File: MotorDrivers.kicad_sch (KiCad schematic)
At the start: 0 parts

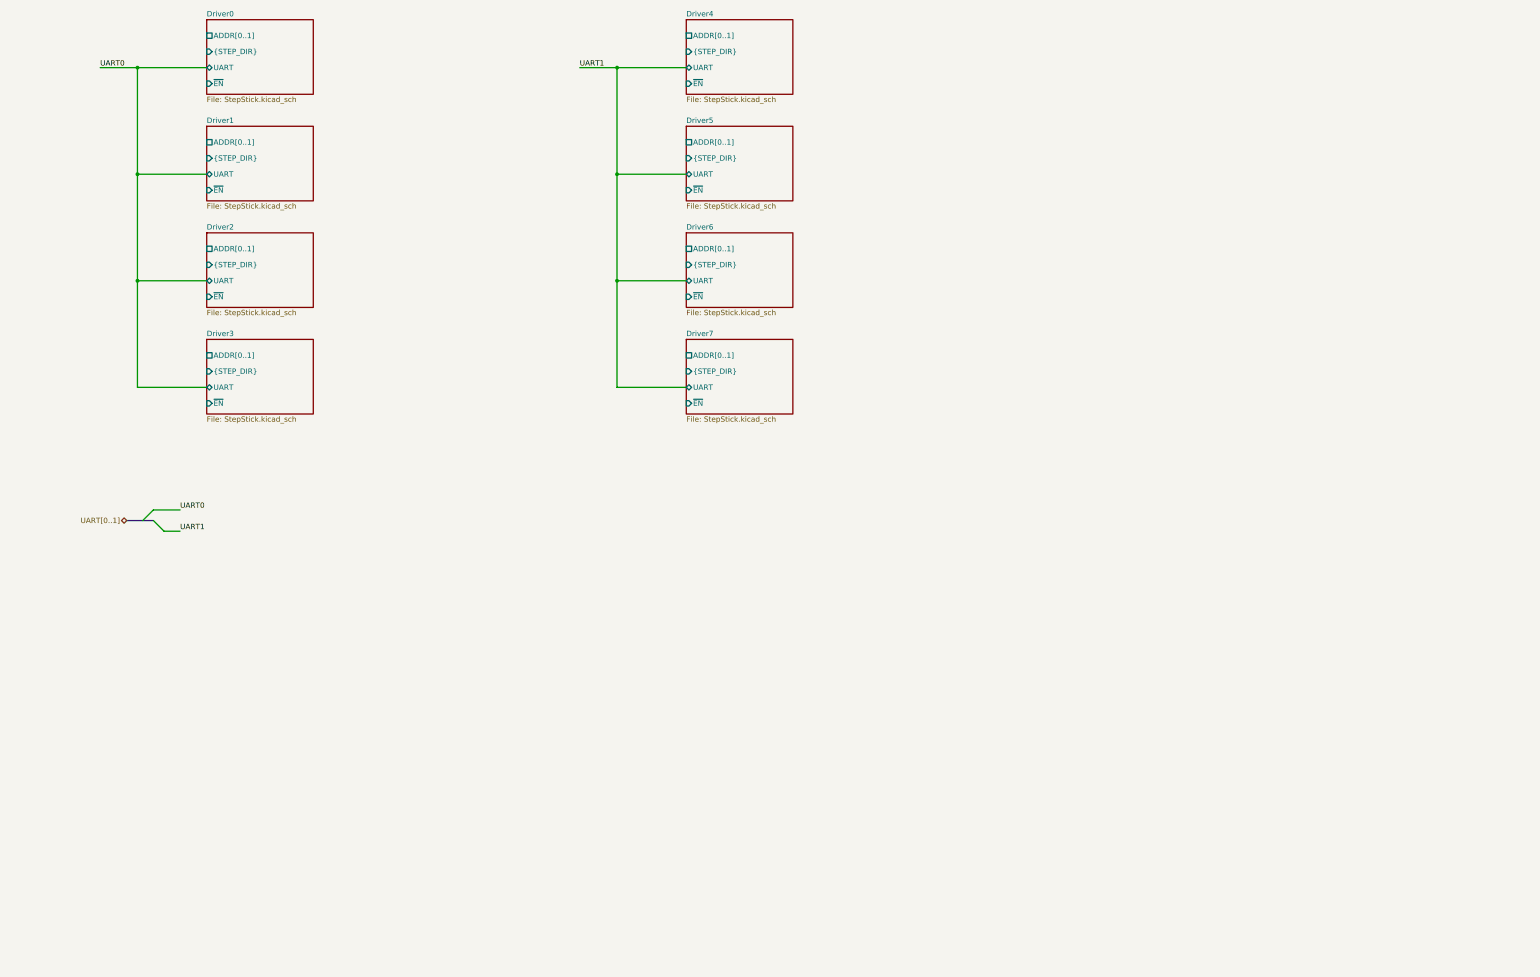
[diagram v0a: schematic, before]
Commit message: Increase text size, redo bus labels
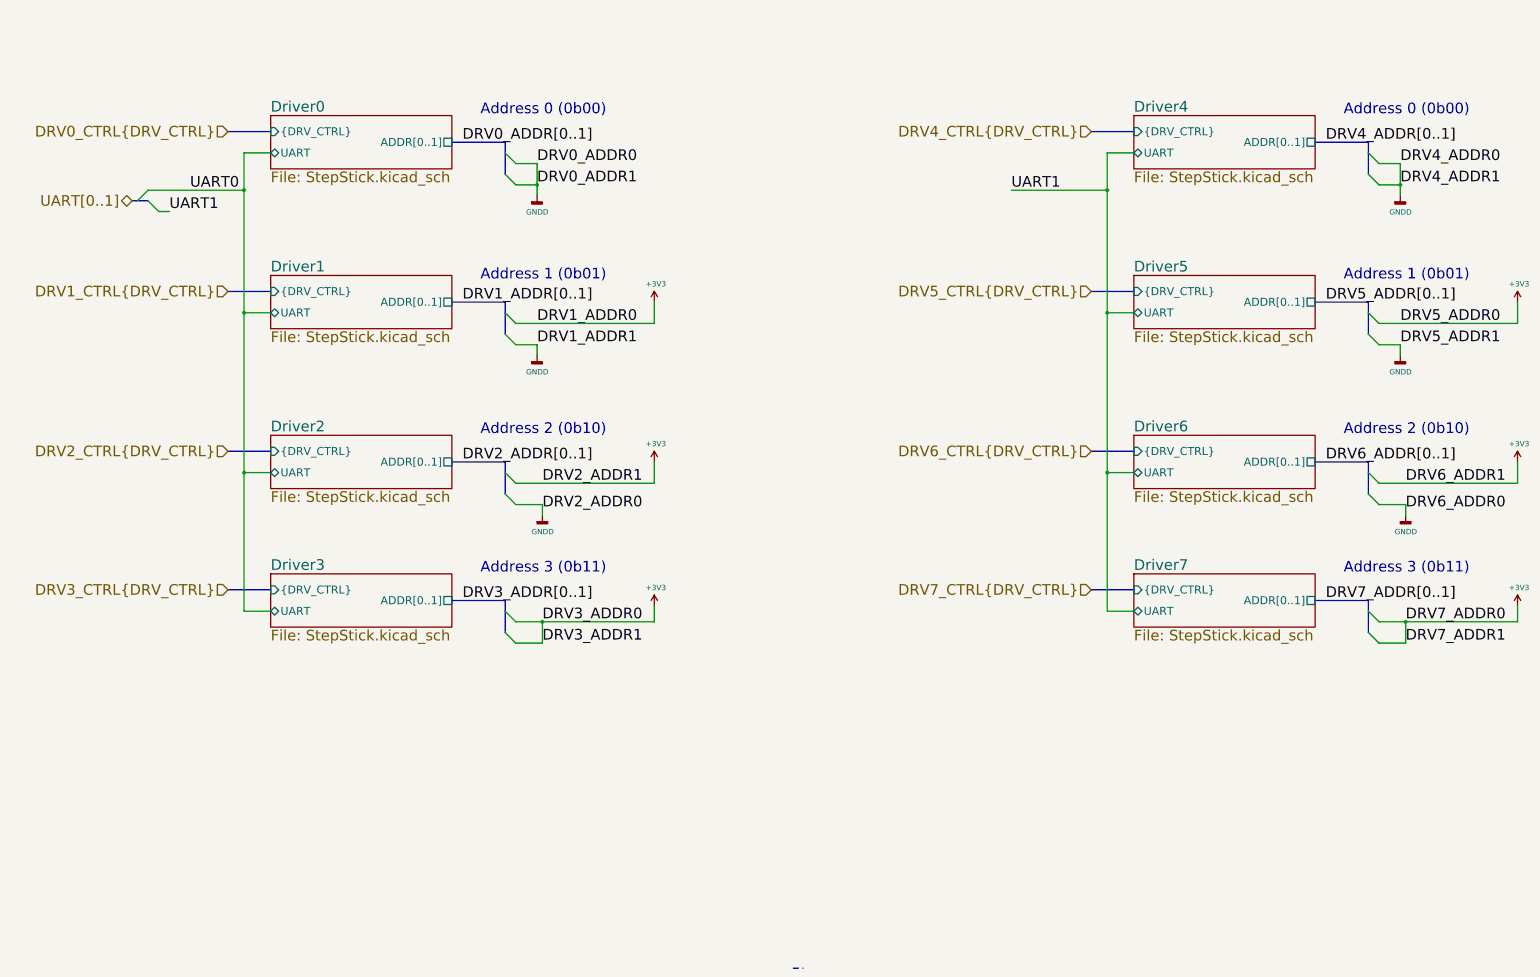
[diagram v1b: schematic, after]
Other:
- sheet Driver0 ports: added {DRV_CTRL}; removed {STEP_DIR}, ~EN
- sheet Driver1 ports: added {DRV_CTRL}; removed {STEP_DIR}, ~EN
- sheet Driver2 ports: added {DRV_CTRL}; removed {STEP_DIR}, ~EN
- sheet Driver3 ports: added {DRV_CTRL}; removed {STEP_DIR}, ~EN
- sheet Driver4 ports: added {DRV_CTRL}; removed {STEP_DIR}, ~EN
- sheet Driver5 ports: added {DRV_CTRL}; removed {STEP_DIR}, ~EN
- sheet Driver6 ports: added {DRV_CTRL}; removed {STEP_DIR}, ~EN
- sheet Driver7 ports: added {DRV_CTRL}; removed {STEP_DIR}, ~EN
- note added: "Address 0 (0b00)"
- note added: "Address 1 (0b01)"
- note added: "Address 2 (0b10)"
- note added: "Address 3 (0b11)"

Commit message: Configure driver chip address with jumpers
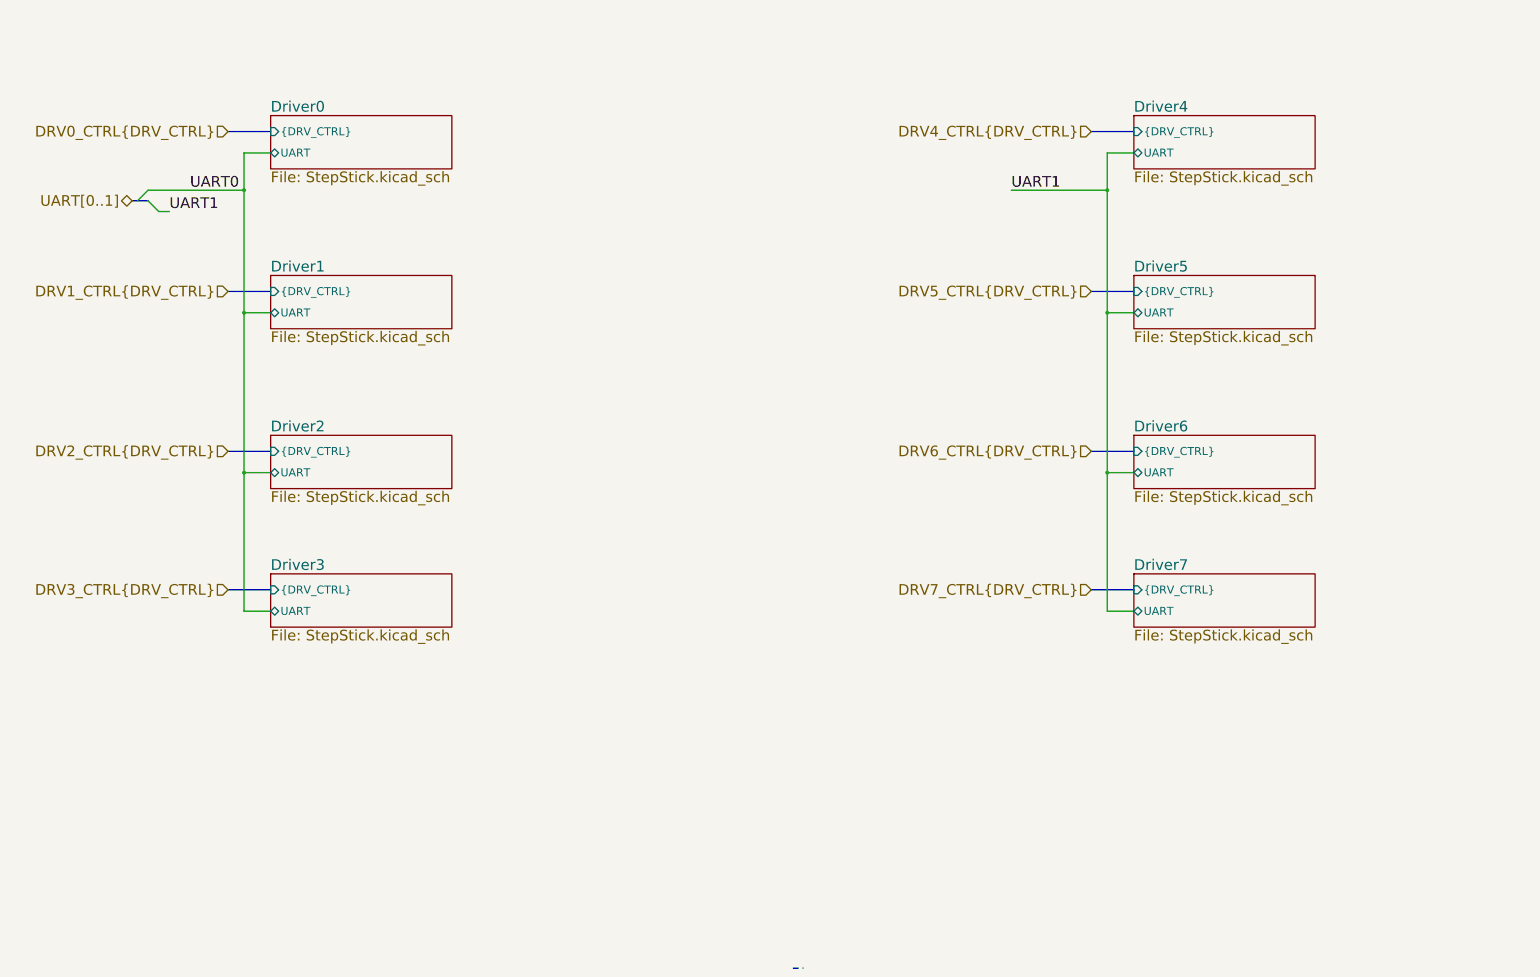
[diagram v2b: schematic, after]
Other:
- sheet Driver0 ports: added none; removed ADDR[0..1]
- sheet Driver1 ports: added none; removed ADDR[0..1]
- sheet Driver2 ports: added none; removed ADDR[0..1]
- sheet Driver3 ports: added none; removed ADDR[0..1]
- sheet Driver4 ports: added none; removed ADDR[0..1]
- sheet Driver5 ports: added none; removed ADDR[0..1]
- sheet Driver6 ports: added none; removed ADDR[0..1]
- sheet Driver7 ports: added none; removed ADDR[0..1]
- note removed: "Address 0 (0b00)"
- note removed: "Address 1 (0b01)"
- note removed: "Address 2 (0b10)"
- note removed: "Address 3 (0b11)"
